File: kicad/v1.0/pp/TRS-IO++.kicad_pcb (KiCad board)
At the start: 2 copper layers, 145.7 x 88.6 mm, 90 parts, among them J1 Conn_02x06_Odd_Even, J13 UART, J2 Interface Connector, J3 TRS-80 M3 Edge Connector, J4 SPEAKER, J5 Conn_02x06_Odd_Even, J6 LED3, J7 HDMI, J8 Programmer, J9 LED4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

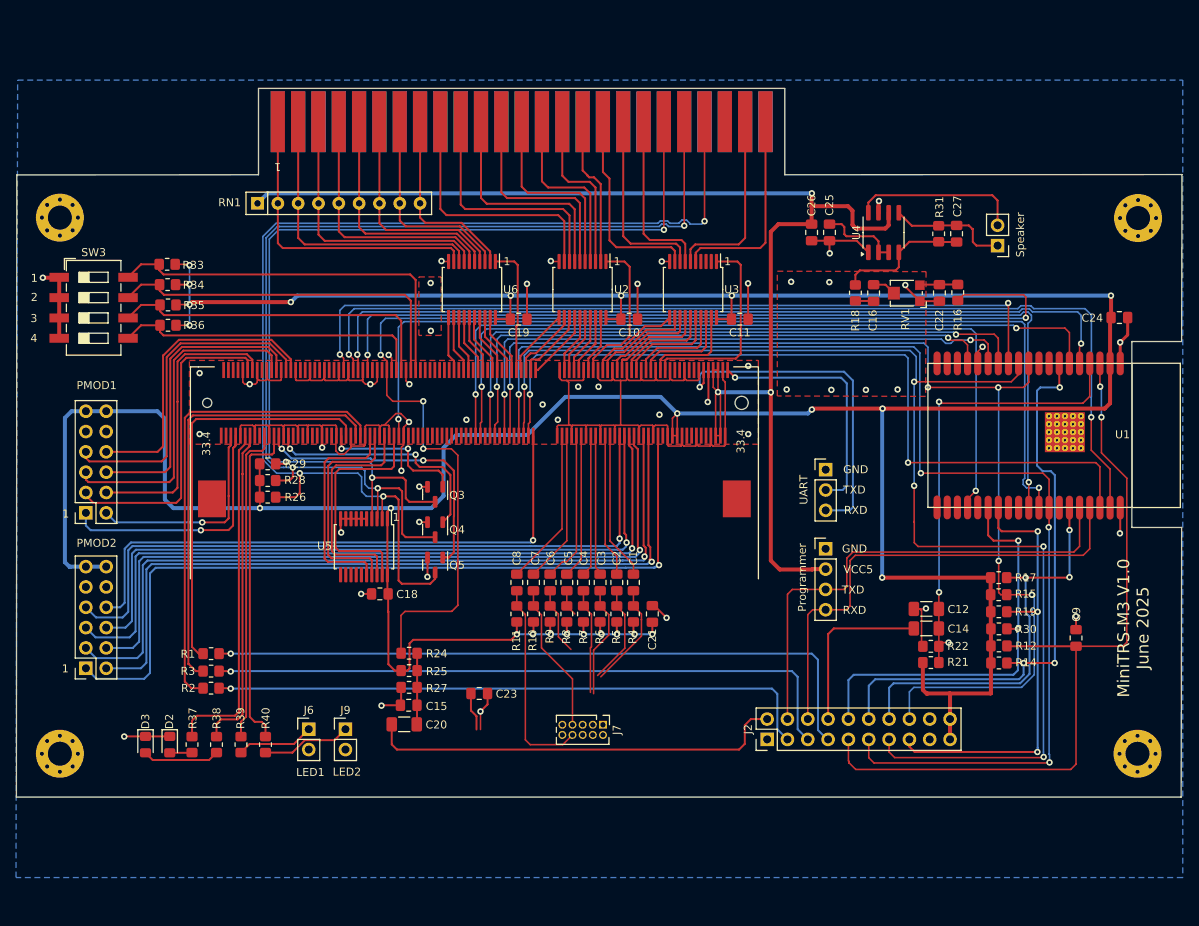
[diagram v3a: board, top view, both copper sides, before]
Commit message: Converted HDMI connector to SMD.
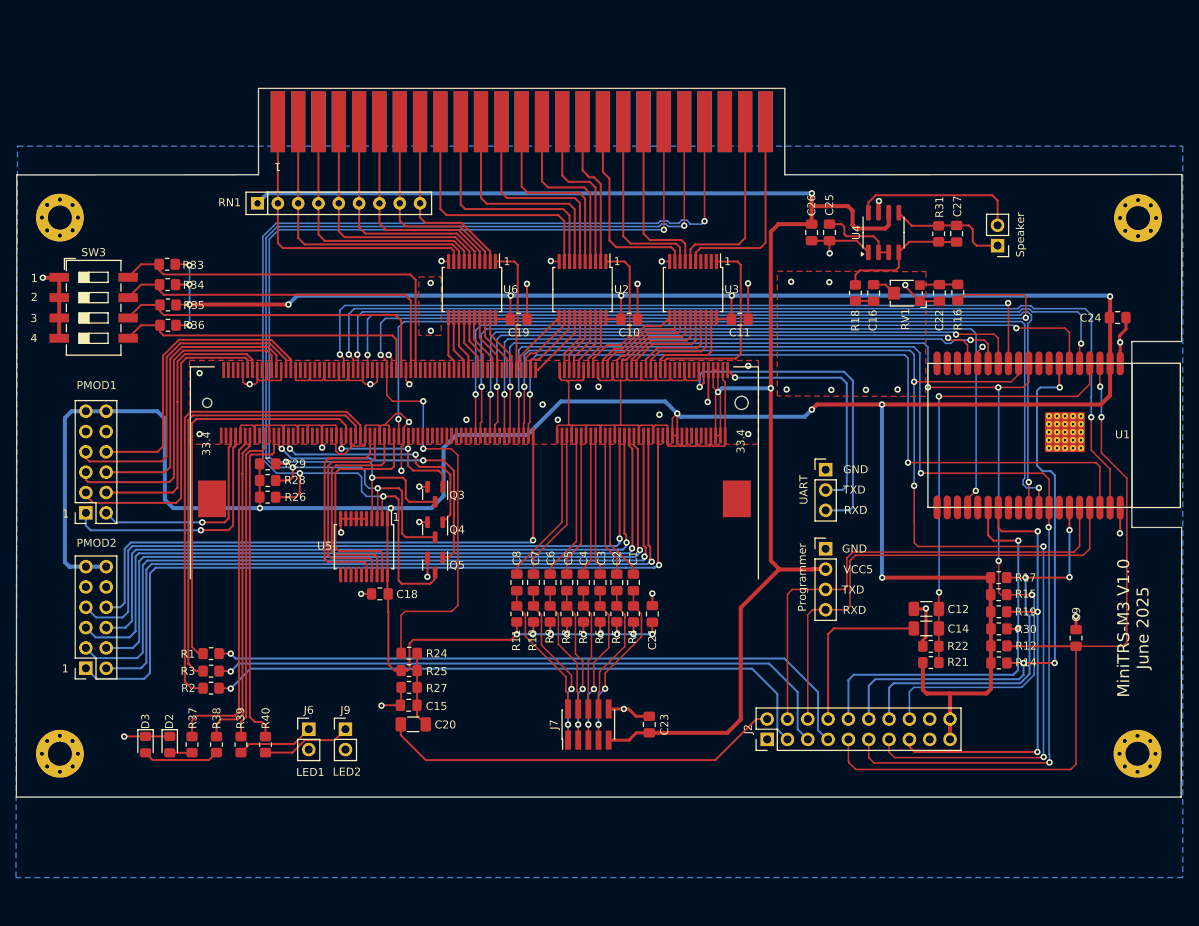
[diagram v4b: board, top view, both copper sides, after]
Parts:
- J7: footprint Connector_PinHeader_1.27mm:PinHeader_2x05_P1.27mm_Vertical -> Connector_PinHeader_1.27mm:PinHeader_2x05_P1.27mm_Vertical_SMD
- moved C23 21.6 mm to (139.7, 127.6), turned to 90 degrees
- moved J7 1.83 mm to (132.1, 127.6), turned to 90 degrees
- moved C20 1.13 mm to (110.2, 127.6)
- moved C24 0.21 mm to (198.2, 76.8)
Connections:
- J7 pad 1: /D2+ -> /CK+
- J7 pad 2: /D2- -> /CK-
- J7 pad 3: /D1+ -> /D0+
- J7 pad 4: /D1- -> /D0-
- J7 pad 5: /D0+ -> /D1+
- J7 pad 6: /D0- -> /D1-
- J7 pad 7: /CK+ -> /D2+
- J7 pad 8: /CK- -> /D2-
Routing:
- net +5V: track 170.7 -> 204.4 mm
- net /D0+: track 3.31 -> 19.7 mm, vias 0 -> 2
- net /CK-: track 25.7 -> 17.4 mm
- net /D2+: track 13.3 -> 21.3 mm, vias 0 -> 2
- net /D0-: track 8.40 -> 16.2 mm
- net /D1+: track 14.1 -> 20.2 mm, vias 0 -> 2
- net /D2-: track 12.4 -> 16.5 mm
- net IF_LED_RED: track 85.7 -> 83.4 mm
- net /D1-: track 13.1 -> 15.3 mm
- net IF_CASS_OUT: track 52.6 -> 50.6 mm
- net IF_LED_GREEN: track 76.3 -> 78.4 mm
- net /CK+: track 18.7 -> 20.7 mm, vias 0 -> 2
- net CASS_IN: track 57.3 -> 55.3 mm, vias 3 -> 2
- net GND: track 265.6 -> 264.4 mm
- net +3V3: track 484.0 -> 483.2 mm

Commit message: First version of MiniTRS PCB
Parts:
- J2: footprint Connector_PinHeader_2.54mm:PinHeader_2x10_P2.54mm_Vertical -> Connector_PinHeader_1.27mm:PinHeader_2x10_P1.27mm_Vertical
- moved J2 8.17 mm to (162.5, 128.0)
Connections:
- J2 pad 1: unconnected-(J2-Pin_1-Pad1) -> IF_CASS_OUT
- J2 pad 2: IF_CASS_OUT -> GND
- J2 pad 3: IF_LED_GREEN -> IF_LED_RED
- J2 pad 7: IF_LED_RED -> IF_LED_GREEN
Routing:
- net IF_LED_GREEN: track 78.4 -> 96.1 mm
- net IF_LED_BLUE: track 80.7 -> 93.2 mm
- net IF_CASS_OUT: track 50.6 -> 61.4 mm
- net IF_LED_RED: track 83.4 -> 91.2 mm
- net IF_CASS_IN: track 21.6 -> 17.2 mm
- net GND: track 264.4 -> 267.7 mm, vias 50 -> 51
- net ID0: track 51.7 -> 48.5 mm
- net +5V: track 204.4 -> 207.2 mm
- net CD_SD: track 56.3 -> 58.8 mm
- net IF_RXD0: track 60.2 -> 58.3 mm
- net IF_BTN_TRSIO_STATUS: track 73.1 -> 71.3 mm
- net +3V3: track 483.2 -> 481.9 mm
- net ESP_RESET: track 98.2 -> 96.9 mm
- net IF_SD_SCK: track 160.1 -> 161.4 mm
- net CS_SD: track 51.0 -> 50.3 mm
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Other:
- board text added: "HDMI"
- board text added: "Interface Panel"
- board text added: "MiniTRS-M3 V1.0 August 2025"
- board text removed: "MiniTRS-M3 V1.0 June 2025"

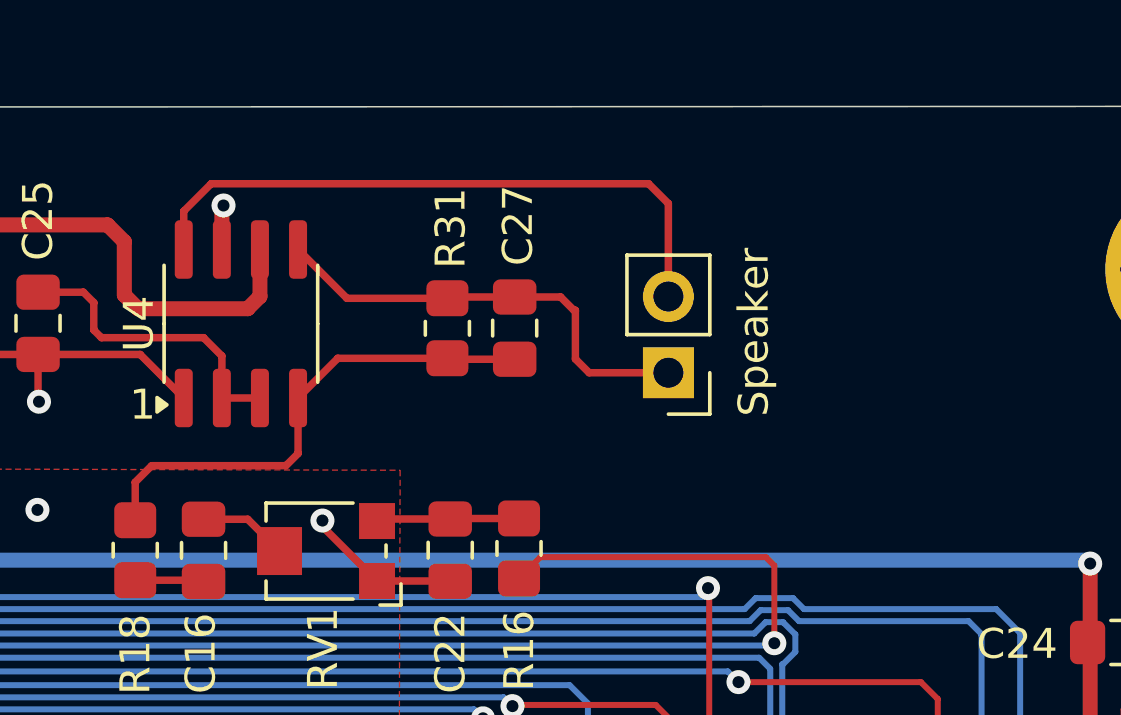
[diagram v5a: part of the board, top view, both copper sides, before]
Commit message: Changed J4 connector for speaker
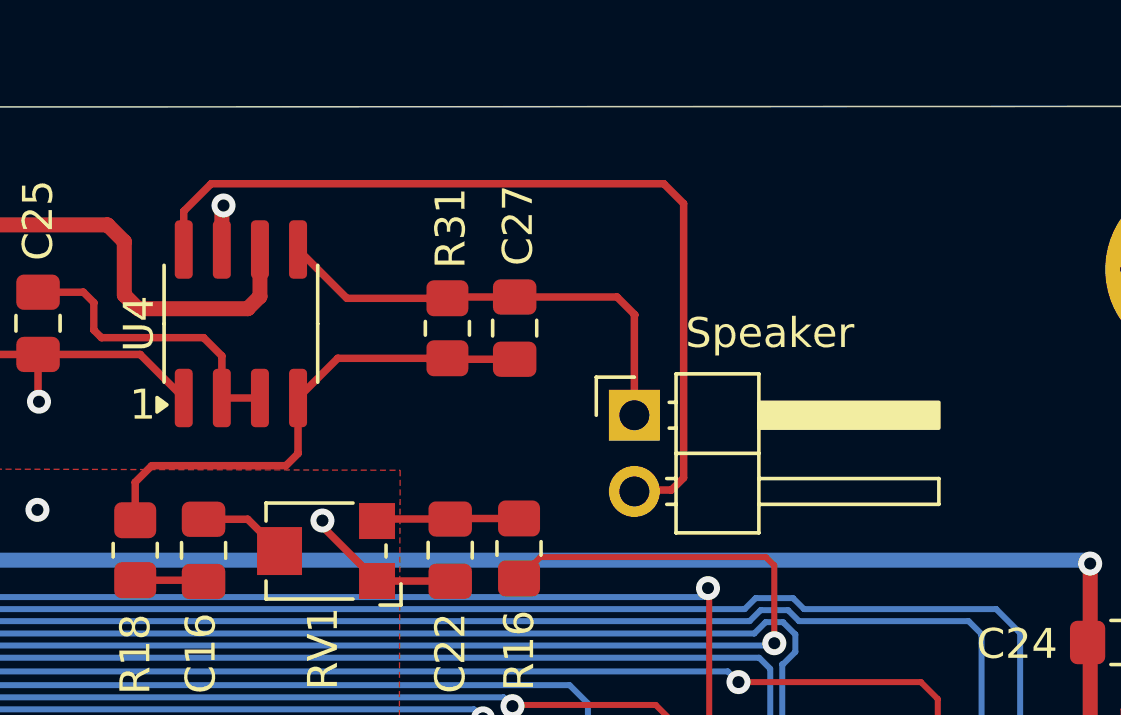
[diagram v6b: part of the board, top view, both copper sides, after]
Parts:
- C22, C27: value 150 -> 150pF
- J4: footprint Connector_PinHeader_2.54mm:PinHeader_1x02_P2.54mm_Vertical -> Connector_PinHeader_2.54mm:PinHeader_1x02_P2.54mm_Horizontal
- moved J4 1.82 mm to (182.1, 69.2), turned to 0 degrees
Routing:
- net Net-(J4-Pin_2): track 21.2 -> 29.6 mm

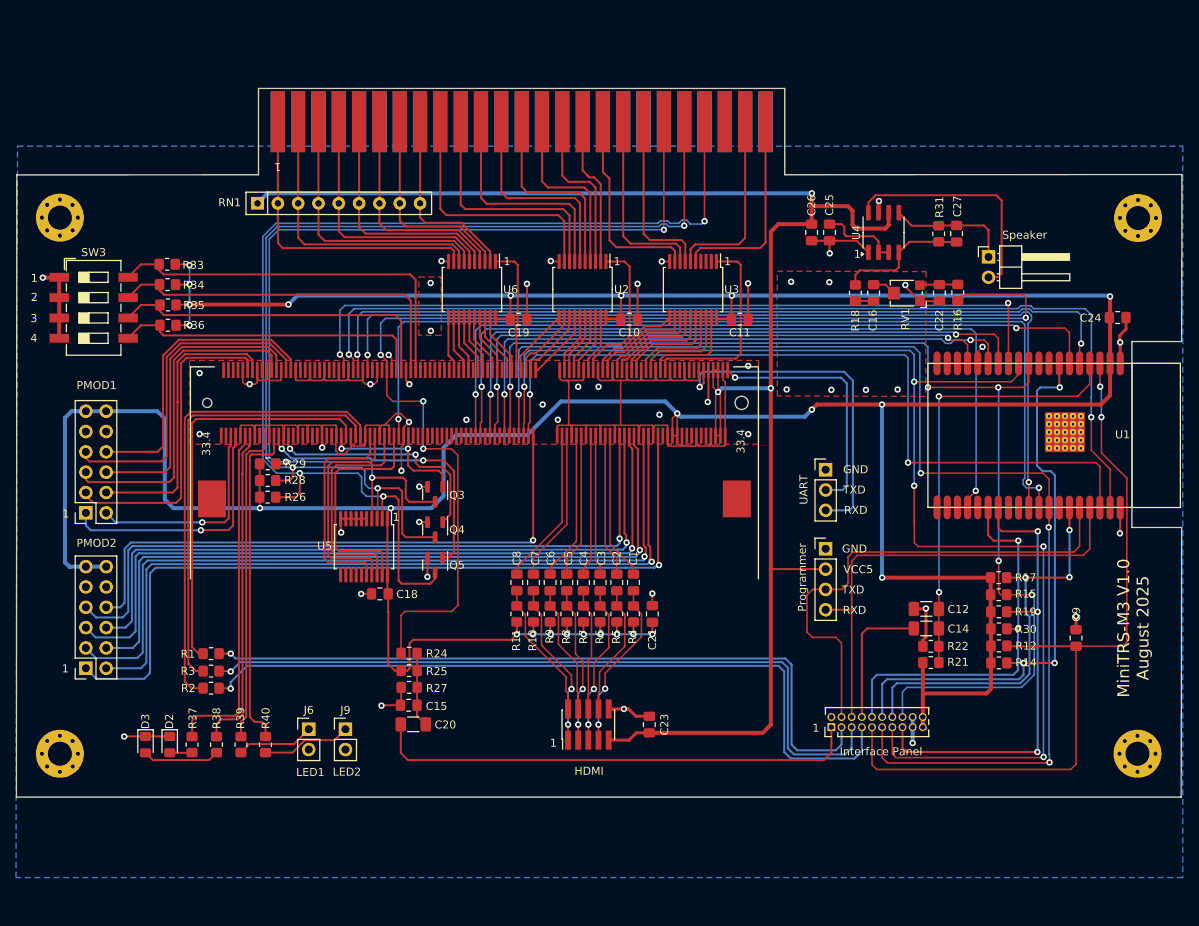
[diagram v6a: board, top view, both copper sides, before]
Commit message: Minor cleanup to PCB to improve ground fill.
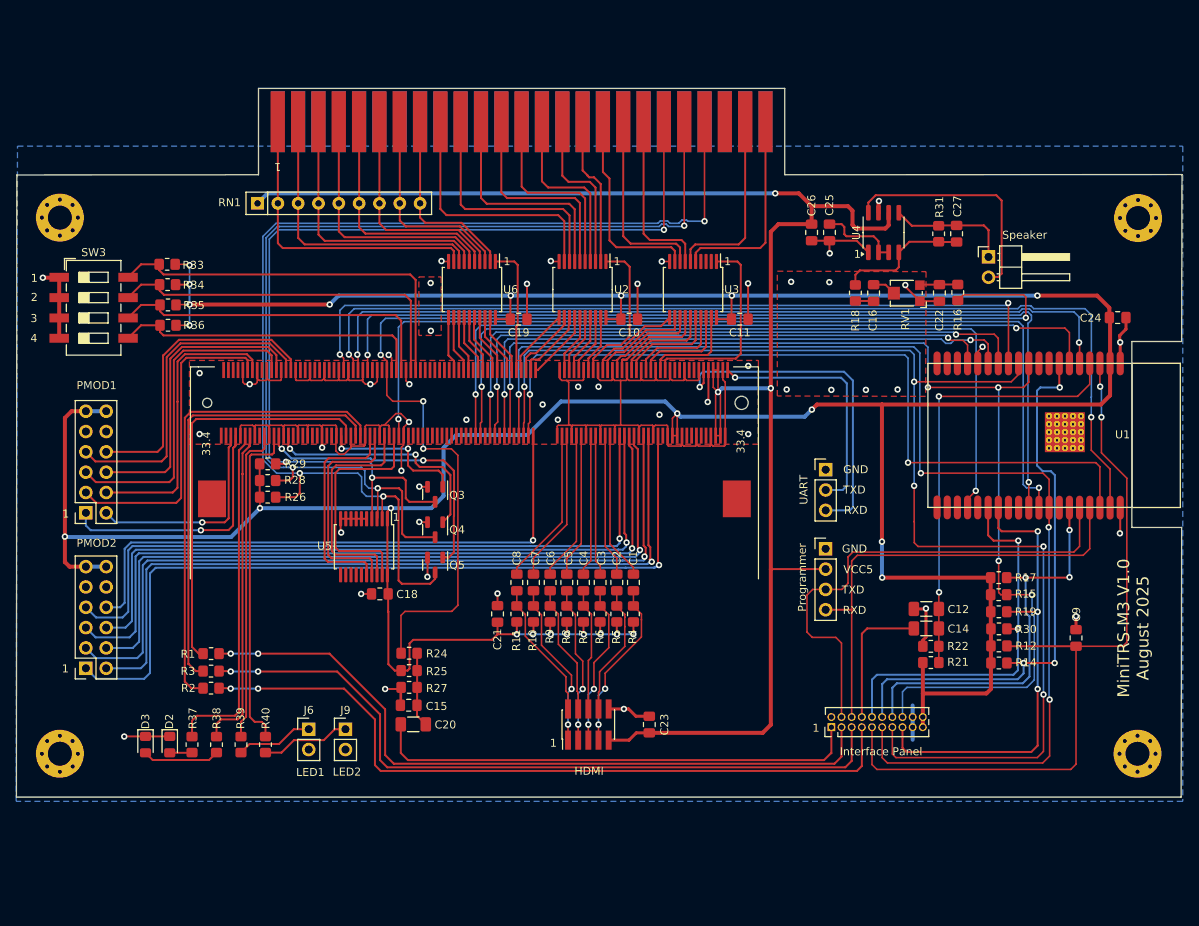
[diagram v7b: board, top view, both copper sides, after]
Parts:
- moved C21 19.4 mm to (120.7, 113.8)
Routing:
- net +3V3: track 481.9 -> 474.3 mm
- net IF_LED_GREEN: track 96.1 -> 93.1 mm, vias 1 -> 2
- net GND: track 267.7 -> 270.3 mm, vias 51 -> 50
- net IF_LED_BLUE: track 93.2 -> 92.0 mm, vias 1 -> 2
- net +5V: track 207.2 -> 206.2 mm
- net PMOD1_IO3: track 41.8 -> 41.2 mm
- net IF_LED_RED: track 91.2 -> 90.9 mm, vias 1 -> 2
